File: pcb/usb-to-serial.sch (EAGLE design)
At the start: 34 parts, among them CON1 MLW10G, IC1 FT231XS, IC2 STMPS2141STR, IC3 CAT6219-330TDGT3, J1 MINI B, J2 MICRO B, J3 EXT

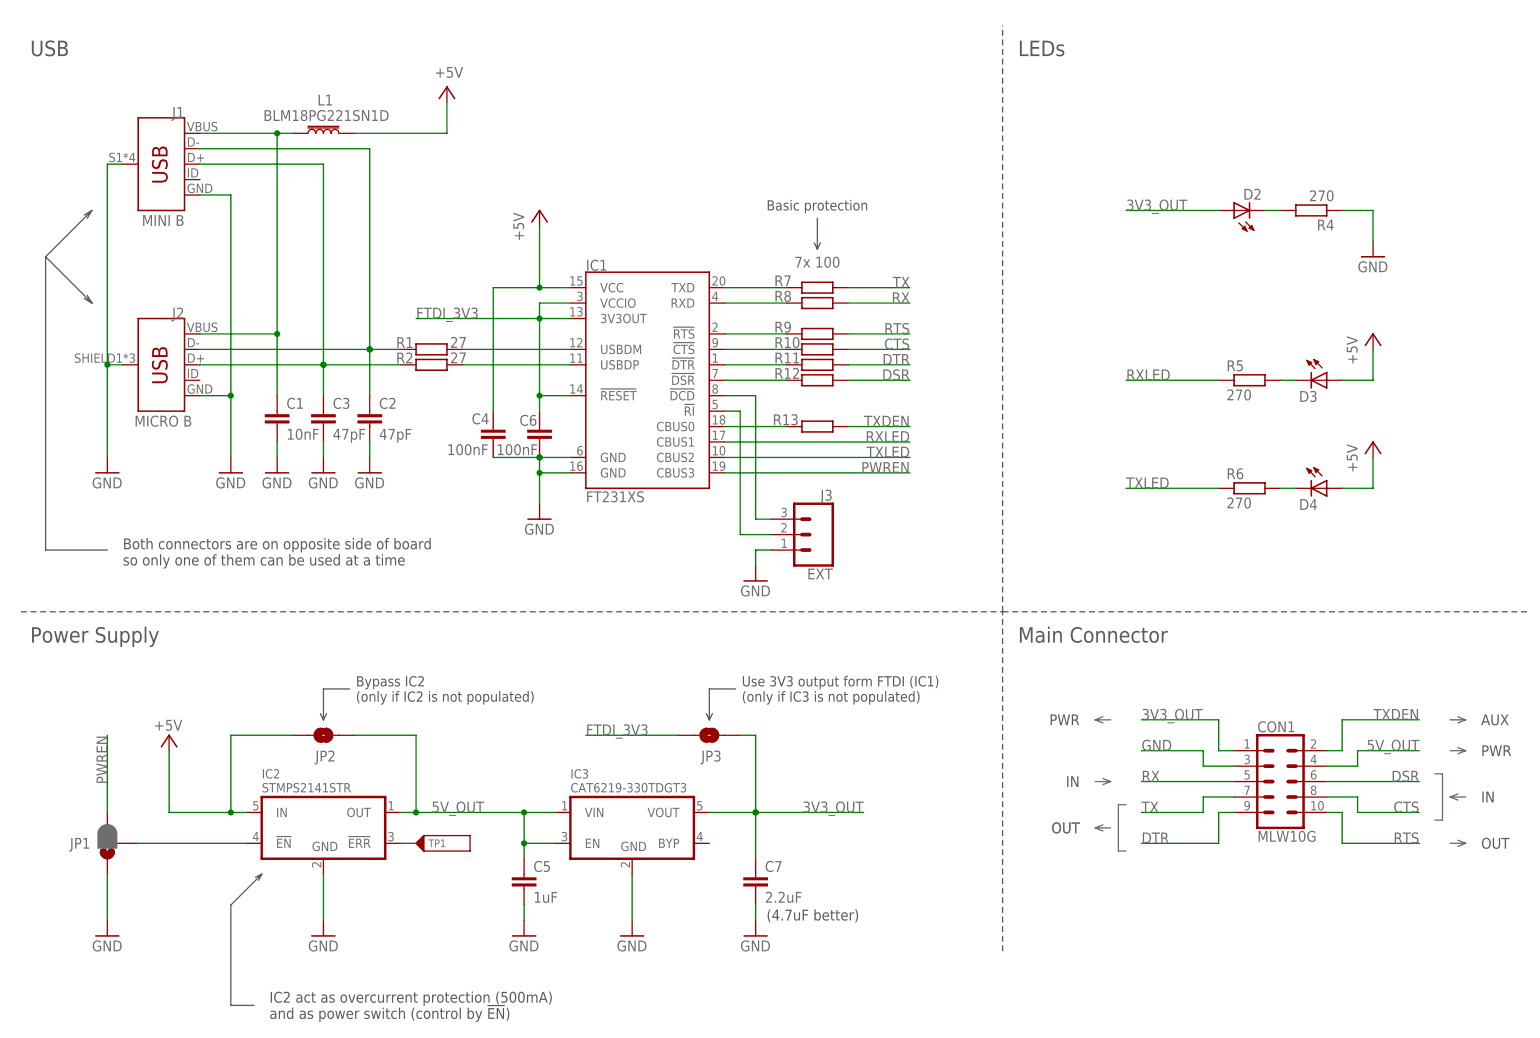
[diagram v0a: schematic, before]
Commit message: Dev v2 merge to master (#1)
* Update to v2

Changes from Issues:
- Pinout on top/bottom silkscreen
- Add indication LED to error output of IC2 (over current shutdown)
- Add EN pin of IC2 to EXT connector
- Add OSHW logo to silkscreen
Replace mini USB connector with USB-C
- Replace IC3 with XC6210

* Polishing of v2 according to notes from Adam, added schematic in PDF, gerber ZIP package.

* Update of BOM for v2 with Farnell links and prices

* 3D models added, update of Readme and kit manual for v2.

* Update of documentation pictures, readme
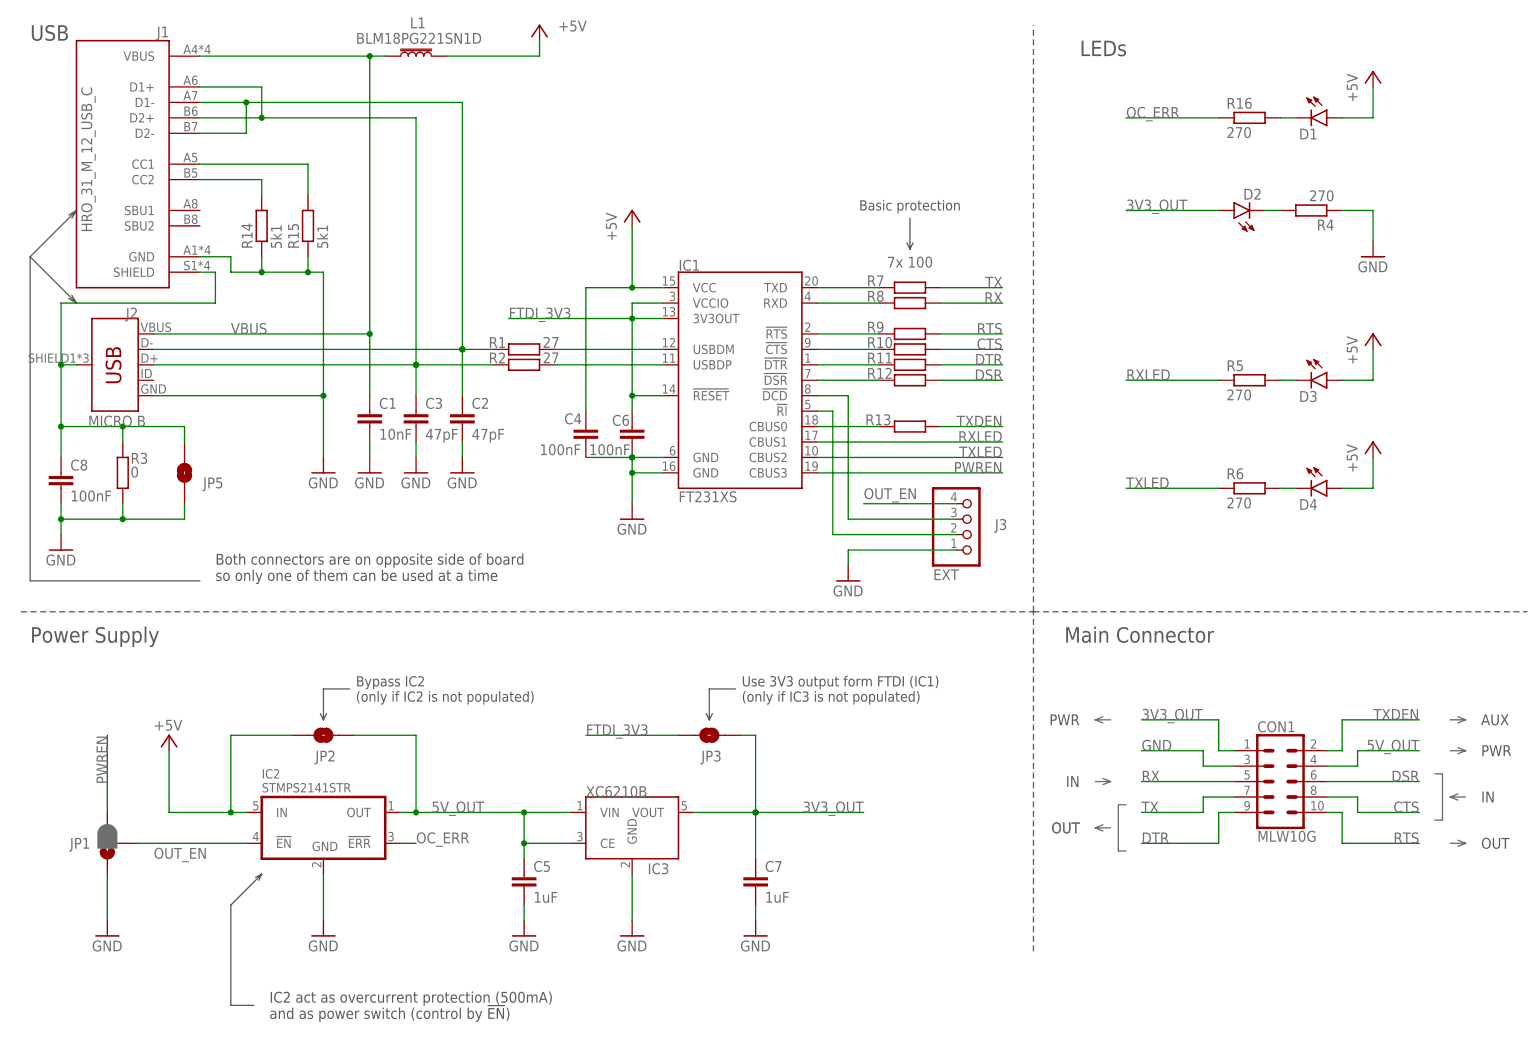
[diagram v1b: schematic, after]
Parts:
- removed J3: EXT, SparkFun-Connectors:CONN_03
- removed TP1: TEST_POINT-1.5, testpoints:TEST_POINT-1.5
- added C8: 100nF, rcl:C-EUC0603
- added D1: (no value), led:LEDCHIP-LED0805
- added EXT: J3, pinhead:PINHD-1X4
- added JP5: JUMPER-SMT_2_NO_NO-SILK, SparkFun-Jumpers:JUMPER-SMT_2_NO_NO-SILK
- added R14, R15: 5k1, rcl:R-EU_R0603
- added R16: 270, rcl:R-EU_R0603
- added R3: 0, rcl:R-EU_R0603
- C7: value 2.2uF -> 1uF
- IC3: value CAT6219-330TDGT3 -> XC6210B332MR; device ic-power:CAT6219-330TDGT3 -> Bastlir:XC6210
- J1: value MINI B -> HRO_31_M_12_USB_C; device SparkFun-Connectors:USB_MINI-B_SMT -> Bastlir:HRO_31_M_12_USB_C
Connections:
- net N$4 renamed VBUS
- removed net N$6: IC2.!ERR, TP1.TP
- new net N$11: D1.C, R16.2
- new net N$7: J1.CC2, R14.2
- new net N$8: C8.1, J1.SHIELD, J2.SHIELD, JP5.2, R3.2
- new net OC_ERR: IC2.!ERR, R16.1
- new net OUT_EN: EXT.4, IC2.!EN, JP1.2
- net +5V: now also D1.A
- net 5V_OUT: now also IC3.CE; no longer IC3.EN
- net DCD: now also EXT.3; no longer J3.3
- net GND: now also C8.2, EXT.1, JP5.1, R14.1, R15.1, R3.1; no longer J1.SHIELD, J2.SHIELD, J3.1
- net N$2: now also J1.CC1, R15.2; no longer IC2.!EN, JP1.2
- net RI: now also EXT.2; no longer J3.2
- net USBD_N: now also J1.D1-, J1.D2-; no longer J1.D-
- net USBD_P: now also J1.D1+, J1.D2+; no longer J1.D+
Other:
- note removed: "(4.7uF better)"
- note removed: "TODO: Rx & Tx LED is switch from defualt config (silk screen)"
- note removed: "TODO: When connect to jut 5V power supply, PWREN is not set => canno be used for just power without USB communication"
- moved on the sheet: C1, C2, C3, C4, C6, IC1, J2, L1, R1, R10, R11, R12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
